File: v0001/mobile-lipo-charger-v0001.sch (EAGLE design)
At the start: 74 parts, among them IC1 AD8610MR, IC3 AD8610MR, IC5 STM32F429NGH, SW2 DHT-4235A, U3 3.3V, U4 3.3V

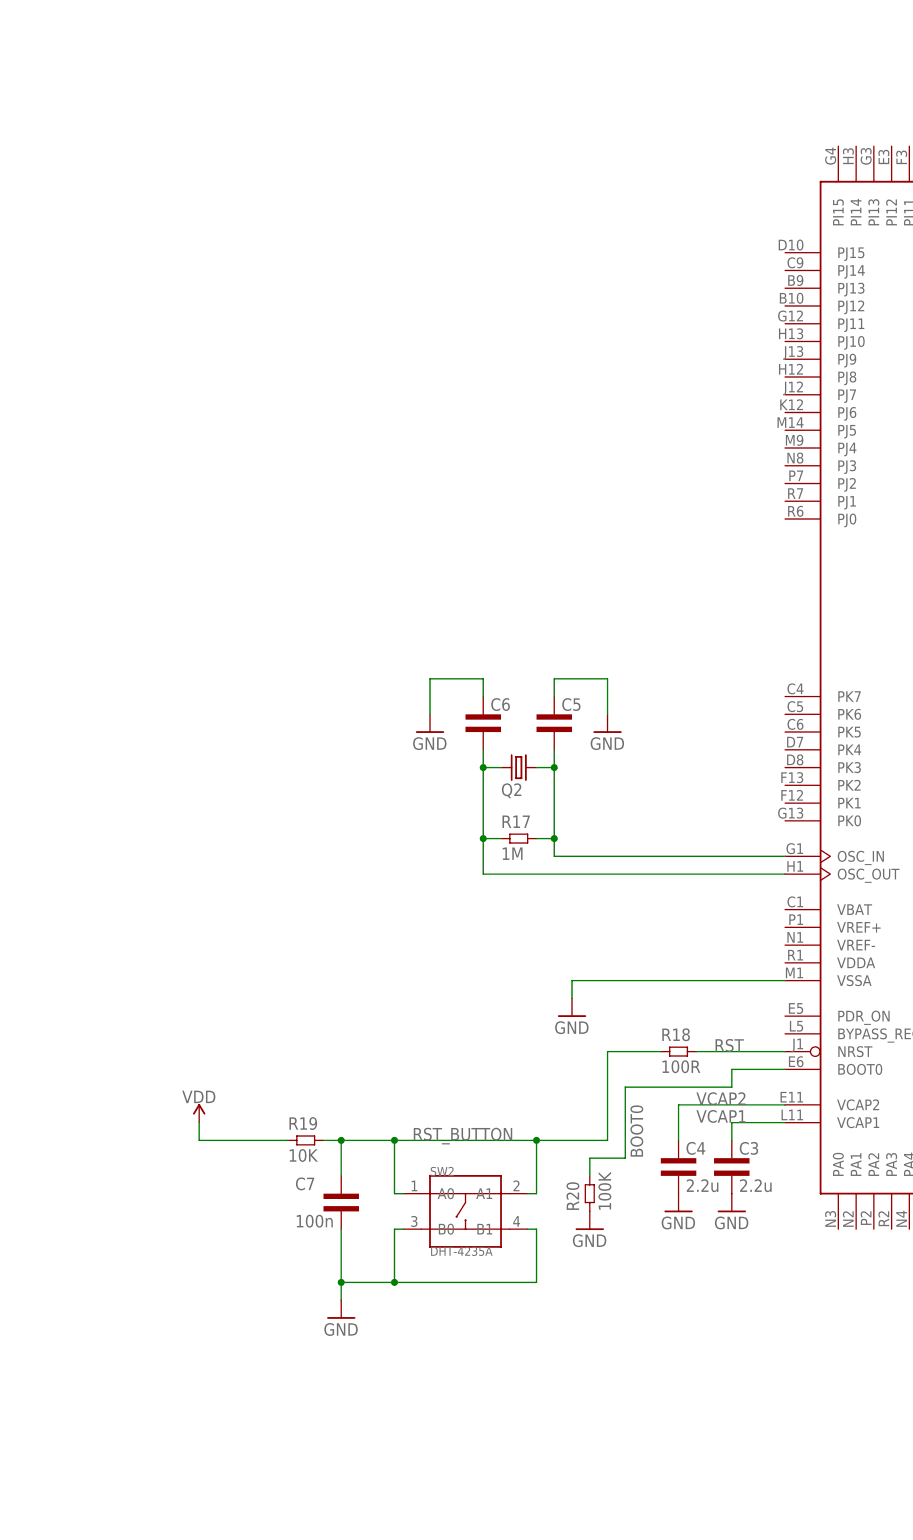
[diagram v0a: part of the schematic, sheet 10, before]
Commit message: Routed
Routed new chip
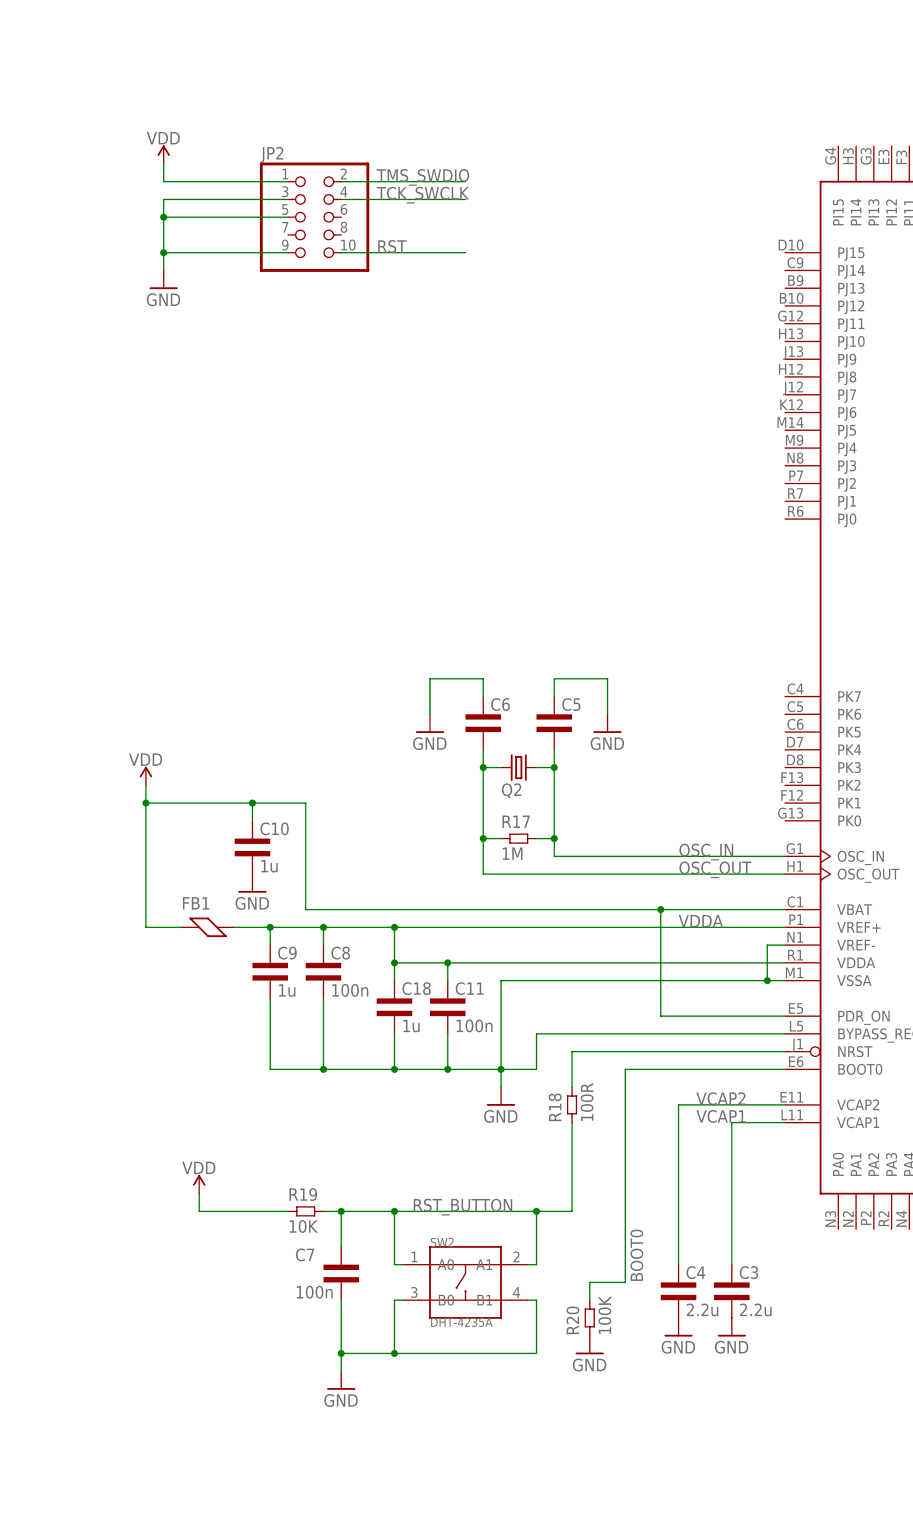
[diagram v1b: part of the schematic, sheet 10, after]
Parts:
- removed C12, C14: 1u, common:CAP0603L3
- removed C13, C15: 100n, common:CAP0402L3
- removed JP1: (no value), pinhead:PINHD-2X5
- added C10, C18, C9: 1u, common:CAP0603L3
- added C11, C8: 100n, common:CAP0402L3
- added FB1: (no value), common:FERRITE0603L3
- added JP2: (no value), pinhead:PINHD-2X5
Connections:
- net N$6 renamed OSC_IN
- net N$7 renamed OSC_OUT
- removed net N$15: C14.1, C15.1
- new net N$3: IC5MCU.NRST, R18.2
- new net VDDA: C11.1, C18.1, C8.1, C9.1, FB1.2, IC5MCU.VDDA, IC5MCU.VREF+
- net GND: now also C10.2, C11.2, C18.2, C8.2, C9.2, IC5MCU.BYPASS_REG, IC5MCU.VREF-, JP2.3, JP2.5, JP2.9; no longer C12.2, C13.2, C14.2, C15.2, JP1.3, JP1.5, JP1.9
- net RST: now also JP2.10; no longer IC5MCU.NRST, JP1.10, R18.2
- net TCK_SWCLK: now also JP2.4; no longer JP1.4
- net TMS_SWDIO: now also JP2.2; no longer JP1.2
- net VDD: now also C10.1, FB1.1, IC5MCU.PDR_ON, IC5MCU.VBAT, JP2.1; no longer C12.1, C13.1, JP1.1
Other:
- moved on the sheet: C3, C4, C7, R18, R19, R20, SW2

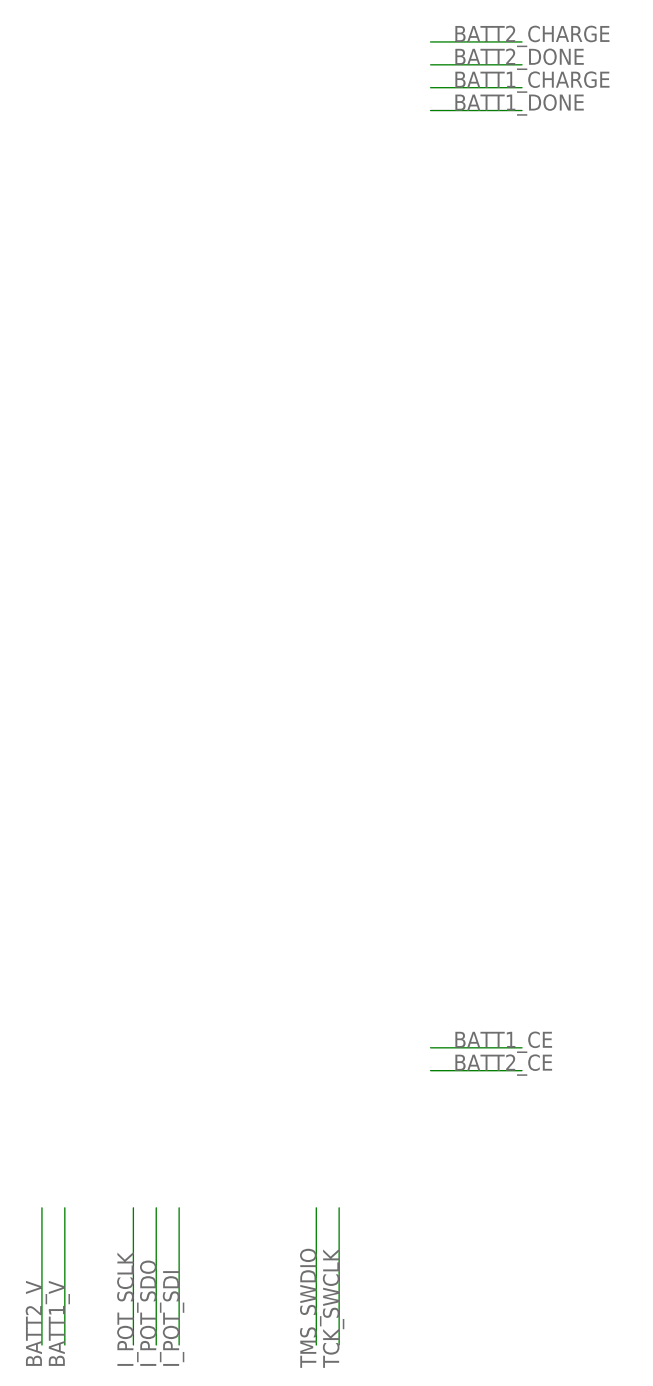
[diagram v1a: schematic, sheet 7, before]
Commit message: Routed ferrite bead
Routed the ferrite bead for VDDA and VREF+
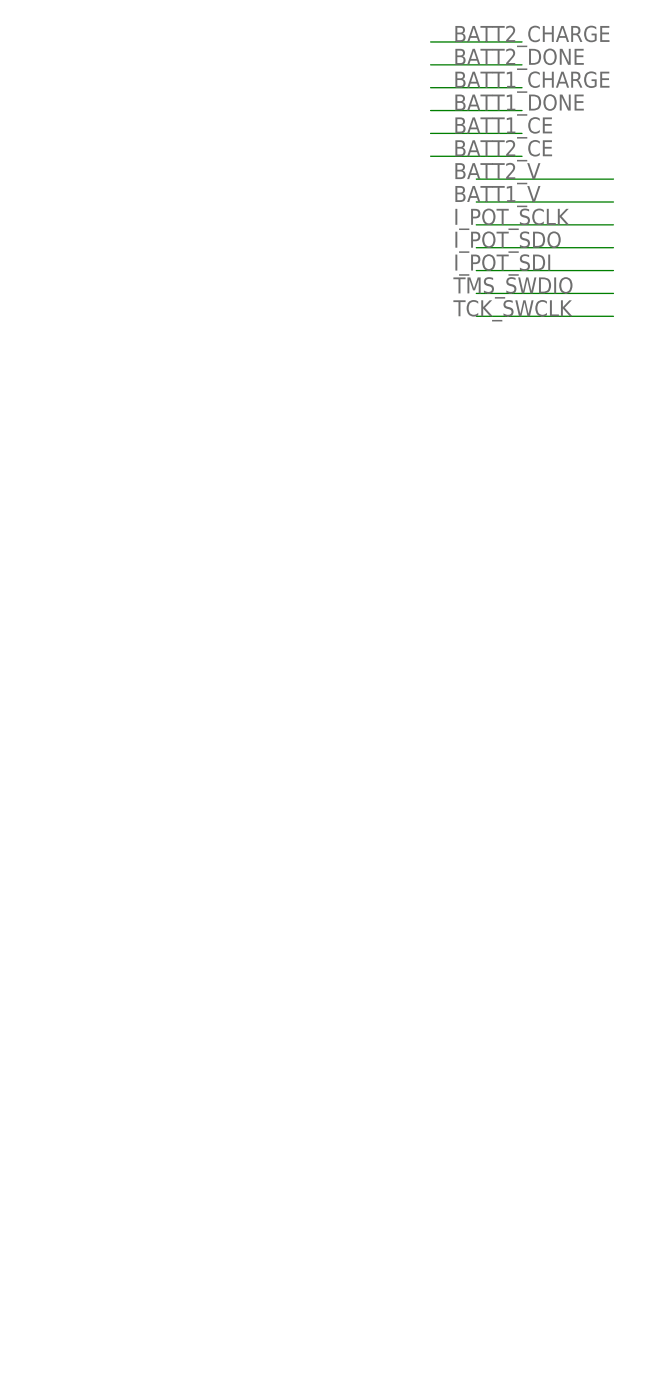
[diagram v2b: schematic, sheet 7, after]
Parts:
- C18, C9: device common:CAP0603L3 -> common:CAP0805L3
- C3, C4: device common:CAP0603L3 -> common:CAP0805L3; DATASHEET (none) -> https://www.mouser.com/datasheet/2/40/TAJ_LOW_PROFILE-93265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; MANUFACTURER (none) -> AVX; PART-NUM (none) -> 581-TAJR225K016RNJ; VENDOR (none) -> mouser.com
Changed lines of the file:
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@@
 <part name="C49" library="rcl" library_urn="urn:adsk.eagle:library:334" deviceset="C-US" device="C0201" package3d_urn="urn:adsk.eagle:package:23690/2" value="100n"/>
 <part name="C50" library="rcl" library_urn="urn:adsk.eagle:library:334" deviceset="C-US" device="C0201" package3d_urn="urn:adsk.eagle:package:23690/2" value="100n"/>
-<part name="C3" library="common" deviceset="CAP" device="0603L3" value="2.2u"/>
-<part name="C4" library="common" deviceset="CAP" device="0603L3" value="2.2u"/>
+<part name="C3" library="common" deviceset="CAP" device="0805L3" value="2.2u">
+<attribute name="DATASHEET" value="https://www.mouser.com/datasheet/2/40/TAJ_LOW_PROFILE-932651.pdf"/>
+<attribute name="MANUFACTURER" value="AVX"/>
+<attribute name="PART-NUM" value="581-TAJR225K016RNJ"/>
+<attribute name="VENDOR" value="mouser.com"/>
+</part>
+<part name="C4" library="common" deviceset="CAP" device="0805L3" value="2.2u">
+<attribute name="DATASHEET" value="https://www.mouser.com/datasheet/2/40/TAJ_LOW_PROFILE-932651.pdf"/>
+<attribute name="MANUFACTURER" value="AVX"/>
+<attribute name="PART-NUM" value="581-TAJR225K016RNJ"/>
+<attribute name="VENDOR" value="mouser.com"/>
+</part>
 <part name="GND9" library="SparkFun-Aesthetics" deviceset="GND" device=""/>
 <part name="GND31" library="SparkFun-Aesthetics" deviceset="GND" device=""/>
@@
 <part name="GND36" library="SparkFun-Aesthetics" deviceset="GND" device=""/>
 <part name="C8" library="common" deviceset="CAP" device="0402L3" value="100n"/>
-<part name="C9" library="common" deviceset="CAP" device="0603L3" value="1u"/>
+<part name="C9" library="common" deviceset="CAP" device="0805L3" value="1u"/>
 <part name="FB1" library="common" deviceset="FERRITE" device="0603L3"/>
 <part name="SUPPLY3" library="SparkFun-PowerSymbols" library_urn="urn:adsk.eagle:library:530" deviceset="VDD" device=""/>
@@
 <part name="GND4" library="SparkFun-Aesthetics" deviceset="GND" device=""/>
 <part name="C11" library="common" deviceset="CAP" device="0402L3" value="100n"/>
-<part name="C18" library="common" deviceset="CAP" device="0603L3" value="1u"/>
+<part name="C18" library="common" deviceset="CAP" device="0805L3" value="1u"/>
 <part name="JP2" library="pinhead" library_urn="urn:adsk.eagle:library:325" deviceset="PINHD-2X5" device="" package3d_urn="urn:adsk.eagle:package:22470/2"/>
 <part name="GND5" library="SparkFun-Aesthetics" deviceset="GND" device=""/>
@@
 <net name="I_POT_SCLK" class="0">
 <segment>
-<wire x1="63.5" y1="-76.2" x2="63.5" y2="-91.44" width="0.1524" layer="91"/>
-<label x="63.5" y="-93.98" size="1.778" layer="95" rot="R90"/>
+<wire x1="116.84" y1="33.02" x2="101.6" y2="33.02" width="0.1524" layer="91"/>
+<label x="99.06" y="33.02" size="1.778" layer="95"/>
 </segment>
 </net>
 <net name="I_POT_SDO" class="0">
 <segment>
-<wire x1="66.04" y1="-91.44" x2="66.04" y2="-76.2" width="0.1524" layer="91"/>
-<label x="66.04" y="-93.98" size="1.778" layer="95" rot="R90"/>
+<wire x1="101.6" y1="30.48" x2="116.84" y2="30.48" width="0.1524" layer="91"/>
+<label x="99.06" y="30.48" size="1.778" layer="95"/>
 </segment>
 </net>
 <net name="I_POT_SDI" class="0">
 <segment>
-<wire x1="68.58" y1="-91.44" x2="68.58" y2="-76.2" width="0.1524" layer="91"/>
-<label x="68.58" y="-93.98" size="1.778" layer="95" rot="R90"/>
+<wire x1="101.6" y1="27.94" x2="116.84" y2="27.94" width="0.1524" layer="91"/>
+<label x="99.06" y="27.94" size="1.778" layer="95"/>
 </segment>
 </net>
 <net name="BATT2_V" class="0">
 <segment>
-<wire x1="53.34" y1="-91.44" x2="53.34" y2="-76.2" width="0.1524" layer="91"/>
-<label x="53.34" y="-93.98" size="1.778" layer="95" rot="R90"/>
+<wire x1="101.6" y1="38.1" x2="116.84" y2="38.1" width="0.1524" layer="91"/>
+<label x="99.06" y="38.1" size="1.778" layer="95"/>
 </segment>
 </net>
 <net name="TMS_SWDIO" class="0">
 <segment>
-<wire x1="83.82" y1="-91.44" x2="83.82" y2="-76.2" width="0.1524" layer="91"/>
-<label x="83.82" y="-93.98" size="1.778" layer="95" rot="R90"/>
+<wire x1="101.6" y1="25.4" x2="116.84" y2="25.4" width="0.1524" layer="91"/>
+<label x="99.06" y="25.4" size="1.778" layer="95"/>
 </segment>
 </net>
 <net name="TCK_SWCLK" class="0">
 <segment>
-<wire x1="86.36" y1="-91.44" x2="86.36" y2="-76.2" width="0.1524" layer="91"/>
-<label x="86.36" y="-93.98" size="1.778" layer="95" rot="R90"/>
+<wire x1="101.6" y1="22.86" x2="116.84" y2="22.86" width="0.1524" layer="91"/>
+<label x="99.06" y="22.86" size="1.778" layer="95"/>
 </segment>
 </net>
 <net name="BATT1_V" class="0">
 <segment>
-<wire x1="55.88" y1="-91.44" x2="55.88" y2="-76.2" width="0.1524" layer="91"/>
-<label x="55.88" y="-93.98" size="1.778" layer="95" rot="R90"/>
+<wire x1="101.6" y1="35.56" x2="116.84" y2="35.56" width="0.1524" layer="91"/>
+<label x="99.06" y="35.56" size="1.778" layer="95"/>
 </segment>
 </net>
 <net name="BATT2_CE" class="0">
 <segment>
-<wire x1="106.68" y1="-60.96" x2="96.52" y2="-60.96" width="0.1524" layer="91"/>
-<label x="99.06" y="-60.96" size="1.778" layer="95"/>
+<wire x1="106.68" y1="40.64" x2="96.52" y2="40.64" width="0.1524" layer="91"/>
+<label x="99.06" y="40.64" size="1.778" layer="95"/>
 </segment>
 </net>
 <net name="BATT1_CE" class="0">
 <segment>
-<wire x1="106.68" y1="-58.42" x2="96.52" y2="-58.42" width="0.1524" layer="91"/>
-<label x="99.06" y="-58.42" size="1.778" layer="95"/>
+<wire x1="106.68" y1="43.18" x2="96.52" y2="43.18" width="0.1524" layer="91"/>
+<label x="99.06" y="43.18" size="1.778" layer="95"/>
 </segment>
 </net>
@@
 <attribute name="NAME" x="-169.164" y="-55.372" size="1.778" layer="95"/>
 <attribute name="VALUE" x="-169.164" y="-60.706" size="1.778" layer="96"/>
+<attribute name="DATASHEET" x="-170.18" y="-55.88" size="1.778" layer="96" display="off"/>
+<attribute name="MANUFACTURER" x="-170.18" y="-55.88" size="1.778" layer="96" display="off"/>
+<attribute name="PART-NUM" x="-170.18" y="-55.88" size="1.778" layer="96" display="off"/>
+<attribute name="VENDOR" x="-170.18" y="-55.88" size="1.778" layer="96" display="off"/>
 </instance>
 <instance part="C4" gate="G$1" x="-177.8" y="-55.88" smashed="yes">
 <attribute name="NAME" x="-176.784" y="-55.372" size="1.778" layer="95"/>
 <attribute name="VALUE" x="-176.784" y="-60.706" size="1.778" layer="96"/>
+<attribute name="DATASHEET" x="-177.8" y="-55.88" size="1.778" layer="96" display="off"/>
+<attribute name="MANUFACTURER" x="-177.8" y="-55.88" size="1.778" layer="96" display="off"/>
+<attribute name="PART-NUM" x="-177.8" y="-55.88" size="1.778" layer="96" display="off"/>
+<attribute name="VENDOR" x="-177.8" y="-55.88" size="1.778" layer="96" display="off"/>
 </instance>
 <instance part="GND9" gate="1" x="-177.8" y="-63.5" smashed="yes">
@@
 <label x="-220.98" y="101.6" size="1.778" layer="95"/>
 </segment>
+<segment>
+<wire x1="-236.22" y1="40.64" x2="-220.98" y2="40.64" width="0.1524" layer="91"/>
+<label x="-238.76" y="40.64" size="1.778" layer="95"/>
+</segment>
 </net>
 <net name="TCK_SWCLK" class="0">
@@
 <wire x1="-208.28" y1="99.06" x2="-226.06" y2="99.06" width="0.1524" layer="91"/>
 <label x="-220.98" y="99.06" size="1.778" layer="95"/>
+</segment>
+<segment>
+<wire x1="-236.22" y1="38.1" x2="-220.98" y2="38.1" width="0.1524" layer="91"/>
+<label x="-238.76" y="38.1" size="1.778" layer="95"/>
 </segment>
 </net>
@@
 </segment>
 </net>
+<net name="I_POT_SCLK" class="0">
+<segment>
+<wire x1="-220.98" y1="48.26" x2="-236.22" y2="48.26" width="0.1524" layer="91"/>
+<label x="-238.76" y="48.26" size="1.778" layer="95"/>
+</segment>
+</net>
+<net name="I_POT_SDO" class="0">
+<segment>
+<wire x1="-236.22" y1="45.72" x2="-220.98" y2="45.72" width="0.1524" layer="91"/>
+<label x="-238.76" y="45.72" size="1.778" layer="95"/>
+</segment>
+</net>
+<net name="I_POT_SDI" class="0">
+<segment>
+<wire x1="-236.22" y1="43.18" x2="-220.98" y2="43.18" width="0.1524" layer="91"/>
+<label x="-238.76" y="43.18" size="1.778" layer="95"/>
+</segment>
+</net>
+<net name="BATT2_V" class="0">
+<segment>
+<wire x1="-236.22" y1="53.34" x2="-220.98" y2="53.34" width="0.1524" layer="91"/>
+<label x="-238.76" y="53.34" size="1.778" layer="95"/>
+</segment>
+</net>
+<net name="BATT1_V" class="0">
+<segment>
+<wire x1="-236.22" y1="50.8" x2="-220.98" y2="50.8" width="0.1524" layer="91"/>
+<label x="-238.76" y="50.8" size="1.778" layer="95"/>
+</segment>
+</net>
+<net name="BATT2_CE" class="0">
+<segment>
+<wire x1="-231.14" y1="55.88" x2="-241.3" y2="55.88" width="0.1524" layer="91"/>
+<label x="-238.76" y="55.88" size="1.778" layer="95"/>
+</segment>
+</net>
+<net name="BATT1_CE" class="0">
+<segment>
+<wire x1="-231.14" y1="58.42" x2="-241.3" y2="58.42" width="0.1524" layer="91"/>
+<label x="-238.76" y="58.42" size="1.778" layer="95"/>
+</segment>
+</net>
+<net name="BATT1_DONE" class="0">
+<segment>
+<wire x1="-241.3" y1="60.96" x2="-231.14" y2="60.96" width="0.1524" layer="91"/>
+<label x="-238.76" y="60.96" size="1.778" layer="95"/>
+</segment>
+</net>
+<net name="BATT1_CHARGE" class="0">
+<segment>
+<wire x1="-231.14" y1="63.5" x2="-241.3" y2="63.5" width="0.1524" layer="91"/>
+<label x="-238.76" y="63.5" size="1.778" layer="95"/>
+</segment>
+</net>
+<net name="BATT2_DONE" class="0">
+<segment>
+<wire x1="-231.14" y1="66.04" x2="-241.3" y2="66.04" width="0.1524" layer="91"/>
+<label x="-238.76" y="66.04" size="1.778" layer="95"/>
+</segment>
+</net>
+<net name="BATT2_CHARGE" class="0">
+<segment>
+<wire x1="-231.14" y1="68.58" x2="-241.3" y2="68.58" width="0.1524" layer="91"/>
+<label x="-238.76" y="68.58" size="1.778" layer="95"/>
+</segment>
+</net>
